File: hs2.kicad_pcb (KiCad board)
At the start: 2 copper layers, 0 parts

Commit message: layout: Components placement
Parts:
- added C1: 47nF, Capacitor_THT:C_Disc_D4.3mm_W1.9mm_P5.00mm, F.Cu at (110.4, 121.7)
- added C10: 1uF, Capacitor_THT:CP_Radial_D5.0mm_P2.50mm, F.Cu at (138.4, 73.9)
- added C11: 1nF, Capacitor_THT:CP_Radial_D5.0mm_P2.50mm, F.Cu at (155.2, 100.1)
- added C12: 1uF, Capacitor_THT:CP_Radial_D5.0mm_P2.50mm, F.Cu at (162.3, 68.3)
- added C13: 470p, Capacitor_THT:C_Disc_D4.3mm_W1.9mm_P5.00mm, F.Cu at (159.2, 104.1)
- added C14: 1.5uF, Capacitor_THT:CP_Radial_D5.0mm_P2.50mm, F.Cu at (126.2, 73.4)
- added C15: 150nF, Capacitor_THT:C_Disc_D4.3mm_W1.9mm_P5.00mm, F.Cu at (144.5, 87.1)
- added C16: 100nF, Capacitor_THT:C_Disc_D4.3mm_W1.9mm_P5.00mm, F.Cu at (144.5, 74.9)
- added C17: 68nF, Capacitor_THT:C_Disc_D4.3mm_W1.9mm_P5.00mm, F.Cu at (123.4, 70.1)
- added C18: 6.8nF, Capacitor_THT:C_Disc_D4.3mm_W1.9mm_P5.00mm, F.Cu at (148.5, 92.5)
- added C19: 4.7nF, Capacitor_THT:C_Disc_D4.3mm_W1.9mm_P5.00mm, F.Cu at (148.0, 72.3)
- added C2: 47nF, Capacitor_THT:C_Disc_D4.3mm_W1.9mm_P5.00mm, F.Cu at (112.2, 95.4)
- added C20: 10uF, Capacitor_THT:CP_Radial_D5.0mm_P2.50mm, F.Cu at (168.3, 101.5)
- added C21: 47n, Capacitor_THT:C_Disc_D4.3mm_W1.9mm_P5.00mm, F.Cu at (154.1, 121.6)
- added C22: 1uF, Capacitor_THT:CP_Radial_D5.0mm_P2.50mm, F.Cu at (168.6, 120.1)
- added C23: 100uF, Capacitor_THT:CP_Radial_D5.0mm_P2.50mm, F.Cu at (154.6, 54.1)
- added C24: 10uF, Capacitor_THT:CP_Radial_D5.0mm_P2.50mm, F.Cu at (133.8, 59.4)
- added C3: 100pF, Capacitor_THT:C_Disc_D4.3mm_W1.9mm_P5.00mm, F.Cu at (111.2, 106.9)
- added C4: 47uF, Capacitor_THT:CP_Radial_D5.0mm_P2.50mm, F.Cu at (111.7, 69.3)
- added C5: 10uF, Capacitor_THT:CP_Radial_D5.0mm_P2.50mm, F.Cu at (107.4, 88.6)
- added C6: 47nF, Capacitor_THT:C_Disc_D4.3mm_W1.9mm_P5.00mm, F.Cu at (104.3, 101.9)
- added C7: 100pF, Capacitor_THT:C_Disc_D4.3mm_W1.9mm_P5.00mm, F.Cu at (138.9, 97.5)
- added C8: 47nF, Capacitor_THT:C_Disc_D4.3mm_W1.9mm_P5.00mm, F.Cu at (120.6, 96.8)
- added C9: 100pF, Capacitor_THT:C_Disc_D4.3mm_W1.9mm_P5.00mm, F.Cu at (155.1, 129.3)
- added D1: 1N4148, Diode_THT:D_DO-35_SOD27_P7.62mm_Horizontal, F.Cu at (144.7, 121.9)
- added D2: 1N4148, Diode_THT:D_DO-35_SOD27_P7.62mm_Horizontal, F.Cu at (141.7, 116.8)
- added D3: 1N4001, Diode_THT:D_DO-41_SOD81_P10.16mm_Horizontal, F.Cu at (151.3, 52.8)
- added D4: 1N4148, Diode_THT:D_DO-35_SOD27_P7.62mm_Horizontal, F.Cu at (141.7, 126.7)
- added D5: DIODE, Diode_THT:D_DO-41_SOD81_P10.16mm_Horizontal, F.Cu at (151.3, 58.7)
- added D6: DIODE, Diode_THT:D_DO-41_SOD81_P10.16mm_Horizontal, F.Cu at (161.5, 62.0)
- added D7: 1N4148, Diode_THT:D_DO-35_SOD27_P7.62mm_Horizontal, F.Cu at (124.9, 125.5)
- added D8: 1N4148, Diode_THT:D_DO-35_SOD27_P7.62mm_Horizontal, F.Cu at (168.1, 68.3)
- added H1: MountingHole_Pad, MountingHole:MountingHole_3.2mm_M3_Pad_TopBottom, F.Cu at (105.4, 54.6)
- added H2: MountingHole_Pad, MountingHole:MountingHole_3.2mm_M3_Pad_TopBottom, F.Cu at (167.8, 54.6)
- added H3: MountingHole_Pad, MountingHole:MountingHole_3.2mm_M3_Pad_TopBottom, F.Cu at (105.4, 132.1)
- added H4: MountingHole_Pad, MountingHole:MountingHole_3.2mm_M3_Pad_TopBottom, F.Cu at (167.8, 132.1)
- added J1: Conn_01x01, Connector_PinHeader_2.54mm:PinHeader_1x01_P2.54mm_Vertical, F.Cu at (103.6, 114.0)
- added J2: Conn_01x01, Connector_PinHeader_2.54mm:PinHeader_1x01_P2.54mm_Vertical, F.Cu at (169.6, 114.0)
- added J3: Conn_01x02, Connector_PinHeader_2.54mm:PinHeader_1x02_P2.54mm_Vertical, F.Cu at (135.3, 53.1)
- added Q1: 2N5457, Package_TO_SOT_THT:TO-92_Inline, F.Cu at (117.5, 114.3)
- added Q2: 2N3904, Package_TO_SOT_THT:TO-92_Inline, F.Cu at (107.5, 107.2)
- added Q3: 2N3906, Package_TO_SOT_THT:TO-92_Inline, F.Cu at (130.0, 87.1)
- added Q4: 2N3904, Package_TO_SOT_THT:TO-92_Inline, F.Cu at (158.4, 120.4)
- added R1: 10k, Resistor_THT:R_Axial_DIN0207_L6.3mm_D2.5mm_P10.16mm_Horizontal, F.Cu at (107.4, 114.0)
- added R10: 10k, Resistor_THT:R_Axial_DIN0207_L6.3mm_D2.5mm_P10.16mm_Horizontal, F.Cu at (111.5, 52.6)
- added R11: 22k, Resistor_THT:R_Axial_DIN0207_L6.3mm_D2.5mm_P10.16mm_Horizontal, F.Cu at (120.6, 94.0)
- added R12: 100k, Resistor_THT:R_Axial_DIN0207_L6.3mm_D2.5mm_P10.16mm_Horizontal, F.Cu at (125.4, 106.9)
- added R13: 470k, Resistor_THT:R_Axial_DIN0207_L6.3mm_D2.5mm_P10.16mm_Horizontal, F.Cu at (135.6, 100.1)
- added R14: 10k, Resistor_THT:R_Axial_DIN0207_L6.3mm_D2.5mm_P10.16mm_Horizontal, F.Cu at (142.2, 100.1)
- added R15: 120, Resistor_THT:R_Axial_DIN0207_L6.3mm_D2.5mm_P10.16mm_Horizontal, F.Cu at (130.8, 90.7)
- added R16: 68k, Resistor_THT:R_Axial_DIN0207_L6.3mm_D2.5mm_P10.16mm_Horizontal, F.Cu at (136.1, 114.0)
- added R17: 47k, Resistor_THT:R_Axial_DIN0207_L6.3mm_D2.5mm_P10.16mm_Horizontal, F.Cu at (117.5, 85.9)
- added R18: 220k, Resistor_THT:R_Axial_DIN0207_L6.3mm_D2.5mm_P10.16mm_Horizontal, F.Cu at (144.7, 124.2)
- added R19: 10k, Resistor_THT:R_Axial_DIN0207_L6.3mm_D2.5mm_P10.16mm_Horizontal, F.Cu at (138.4, 63.0)
- added R2: 1M, Resistor_THT:R_Axial_DIN0207_L6.3mm_D2.5mm_P10.16mm_Horizontal, F.Cu at (113.5, 114.0)
- added R20: 10k, Resistor_THT:R_Axial_DIN0207_L6.3mm_D2.5mm_P10.16mm_Horizontal, F.Cu at (157.9, 73.2)
- added R21: 68k, Resistor_THT:R_Axial_DIN0207_L6.3mm_D2.5mm_P10.16mm_Horizontal, F.Cu at (129.2, 62.7)
- added R22: 3k3, Resistor_THT:R_Axial_DIN0207_L6.3mm_D2.5mm_P10.16mm_Horizontal, F.Cu at (153.4, 92.5)
- added R23: 3k3, Resistor_THT:R_Axial_DIN0207_L6.3mm_D2.5mm_P10.16mm_Horizontal, F.Cu at (156.4, 107.2)
- added R24: 10k, Resistor_THT:R_Axial_DIN0207_L6.3mm_D2.5mm_P10.16mm_Horizontal, F.Cu at (169.4, 95.8)
- added R25: 470k, Resistor_THT:R_Axial_DIN0207_L6.3mm_D2.5mm_P10.16mm_Horizontal, F.Cu at (156.4, 110.5)
- added R26: 10k, Resistor_THT:R_Axial_DIN0207_L6.3mm_D2.5mm_P10.16mm_Horizontal, F.Cu at (168.6, 126.7)
- added R27: 1k, Resistor_THT:R_Axial_DIN0207_L6.3mm_D2.5mm_P10.16mm_Horizontal, F.Cu at (158.4, 123.4)
- added R28: 100k, Resistor_THT:R_Axial_DIN0207_L6.3mm_D2.5mm_P10.16mm_Horizontal, F.Cu at (156.4, 113.8)
- added R29: 100k, Resistor_THT:R_Axial_DIN0207_L6.3mm_D2.5mm_P10.16mm_Horizontal, F.Cu at (113.5, 128.5)
- added R3: 22k, Resistor_THT:R_Axial_DIN0207_L6.3mm_D2.5mm_P10.16mm_Horizontal, F.Cu at (117.5, 98.3)
- added R30: 330, Resistor_THT:R_Axial_DIN0207_L6.3mm_D2.5mm_P10.16mm_Horizontal, F.Cu at (132.0, 74.9)
- added R31: 82k, Resistor_THT:R_Axial_DIN0207_L6.3mm_D2.5mm_P10.16mm_Horizontal, F.Cu at (149.3, 111.3)
- added R32: 330, Resistor_THT:R_Axial_DIN0207_L6.3mm_D2.5mm_P10.16mm_Horizontal, F.Cu at (145.5, 100.1)
- added R33: 100k, Resistor_THT:R_Axial_DIN0207_L6.3mm_D2.5mm_P10.16mm_Horizontal, F.Cu at (135.1, 67.1)
- added R34: 330, Resistor_THT:R_Axial_DIN0207_L6.3mm_D2.5mm_P10.16mm_Horizontal, F.Cu at (151.3, 74.9)
- added R35: 10k, Resistor_THT:R_Axial_DIN0207_L6.3mm_D2.5mm_P10.16mm_Horizontal, F.Cu at (120.9, 56.1)
- added R36: 10k, Resistor_THT:R_Axial_DIN0207_L6.3mm_D2.5mm_P10.16mm_Horizontal, F.Cu at (120.9, 59.4)
- added R38: 330, Resistor_THT:R_Axial_DIN0207_L6.3mm_D2.5mm_P10.16mm_Horizontal, F.Cu at (120.9, 52.8)
- added R4: 10k, Resistor_THT:R_Axial_DIN0207_L6.3mm_D2.5mm_P10.16mm_Horizontal, F.Cu at (122.1, 125.7)
- added R5: 100k, Resistor_THT:R_Axial_DIN0207_L6.3mm_D2.5mm_P10.16mm_Horizontal, F.Cu at (125.4, 119.6)
- added R6: 470k, Resistor_THT:R_Axial_DIN0207_L6.3mm_D2.5mm_P10.16mm_Horizontal, F.Cu at (114.2, 108.5)
- added R7: 22, Resistor_THT:R_Axial_DIN0207_L6.3mm_D2.5mm_P10.16mm_Horizontal, F.Cu at (117.0, 111.3)
- added R8: 150, Resistor_THT:R_Axial_DIN0207_L6.3mm_D2.5mm_P10.16mm_Horizontal, F.Cu at (107.4, 91.7)
- added R9: 1k, Resistor_THT:R_Axial_DIN0207_L6.3mm_D2.5mm_P10.16mm_Horizontal, F.Cu at (115.0, 62.7)
- added U1: Opamp_Dual, Package_SIP:SIP-8_19x3mm_P2.54mm, F.Cu at (136.1, 134.4)
- added U2: Opamp_Dual, Package_SIP:SIP-8_19x3mm_P2.54mm, F.Cu at (148.3, 87.6)
- added U3: Opamp_Dual, Package_SIP:SIP-8_19x3mm_P2.54mm, F.Cu at (149.8, 116.6)
- added VR1: C250k, TerminalBlock:TerminalBlock_bornier-3_P5.08mm, F.Cu at (107.9, 80.3)
- added VR2: B50k, TerminalBlock:TerminalBlock_bornier-3_P5.08mm, F.Cu at (123.6, 80.3)
- added VR3: B50k, TerminalBlock:TerminalBlock_bornier-3_P5.08mm, F.Cu at (139.4, 80.3)
- added VR4: A10k, TerminalBlock:TerminalBlock_bornier-3_P5.08mm, F.Cu at (155.1, 80.3)
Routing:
- net +9V: track 0.00 -> 60.1 mm
- net Net-(C13-Pad2): track 0.00 -> 48.5 mm, vias 0 -> 1
- net GND: track 0.00 -> 47.9 mm
- net Net-(C8-Pad2): track 0.00 -> 40.6 mm
- net Net-(C10-Pad1): track 0.00 -> 33.7 mm
- net Net-(C7-Pad2): track 0.00 -> 30.3 mm
- net Net-(C2-Pad1): track 0.00 -> 27.3 mm
- net /1/2V: track 0.00 -> 21.9 mm
- net Net-(C7-Pad1): track 0.00 -> 20.1 mm
- net Net-(C3-Pad1): track 0.00 -> 19.4 mm
- net Net-(C21-Pad2): track 0.00 -> 17.7 mm
- net Net-(C6-Pad2): track 0.00 -> 17.4 mm
- net Net-(C14-Pad1): track 0.00 -> 15.3 mm
- net Net-(C16-Pad2): track 0.00 -> 13.4 mm
- net Net-(C15-Pad1): track 0.00 -> 12.2 mm
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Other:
- board outline added: 70 x 85 mm

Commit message: layout: Routing finished
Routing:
- net +9V: track 60.1 -> 232.0 mm, vias 0 -> 7
- net /1/2V: track 21.9 -> 148.5 mm, vias 0 -> 5
- net Net-(C17-Pad2): track 0.00 -> 88.9 mm, vias 0 -> 2
- net Net-(C11-Pad1): track 8.13 -> 88.7 mm, vias 0 -> 2
- net Net-(R22-Pad1): track 0.00 -> 75.8 mm, vias 0 -> 2
- net Net-(C13-Pad1): track 4.21 -> 78.4 mm
- net Net-(C12-Pad1): track 0.00 -> 69.6 mm
- net Net-(C19-Pad2): track 2.90 -> 67.9 mm, vias 0 -> 2
- net Net-(C10-Pad1): track 33.7 -> 91.4 mm, vias 0 -> 3
- net Net-(C3-Pad2): track 10.7 -> 65.3 mm
- net Net-(C21-Pad1): track 0.00 -> 52.3 mm
- net Net-(R34-Pad1): track 2.54 -> 50.3 mm, vias 0 -> 1
- net Net-(R32-Pad1): track 2.54 -> 44.3 mm
- net Net-(C18-Pad2): track 0.00 -> 37.3 mm, vias 0 -> 3
- net Net-(C4-Pad1): track 8.09 -> 43.4 mm
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- added copper zone on B.Cu, net GND
- added copper zone on F.Cu, net GND

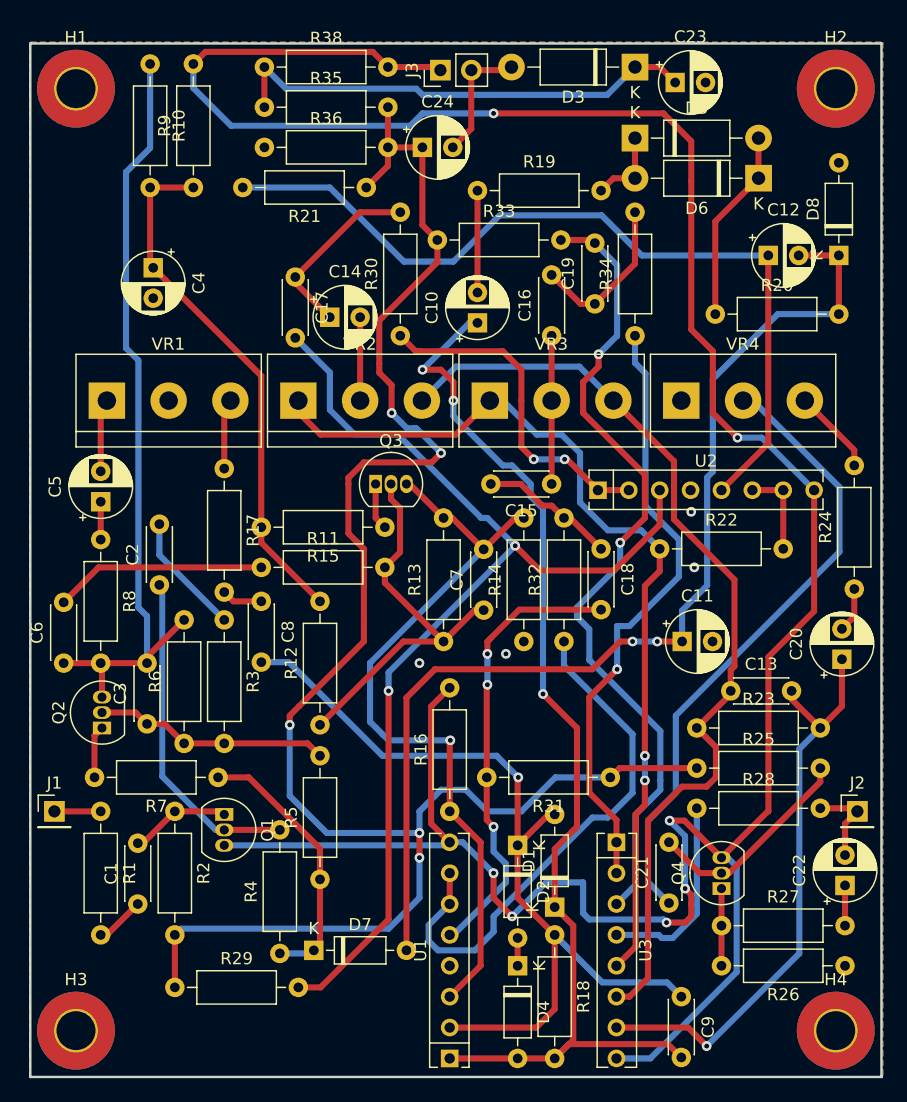
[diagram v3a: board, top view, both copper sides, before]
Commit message: layout: Adding logos and text
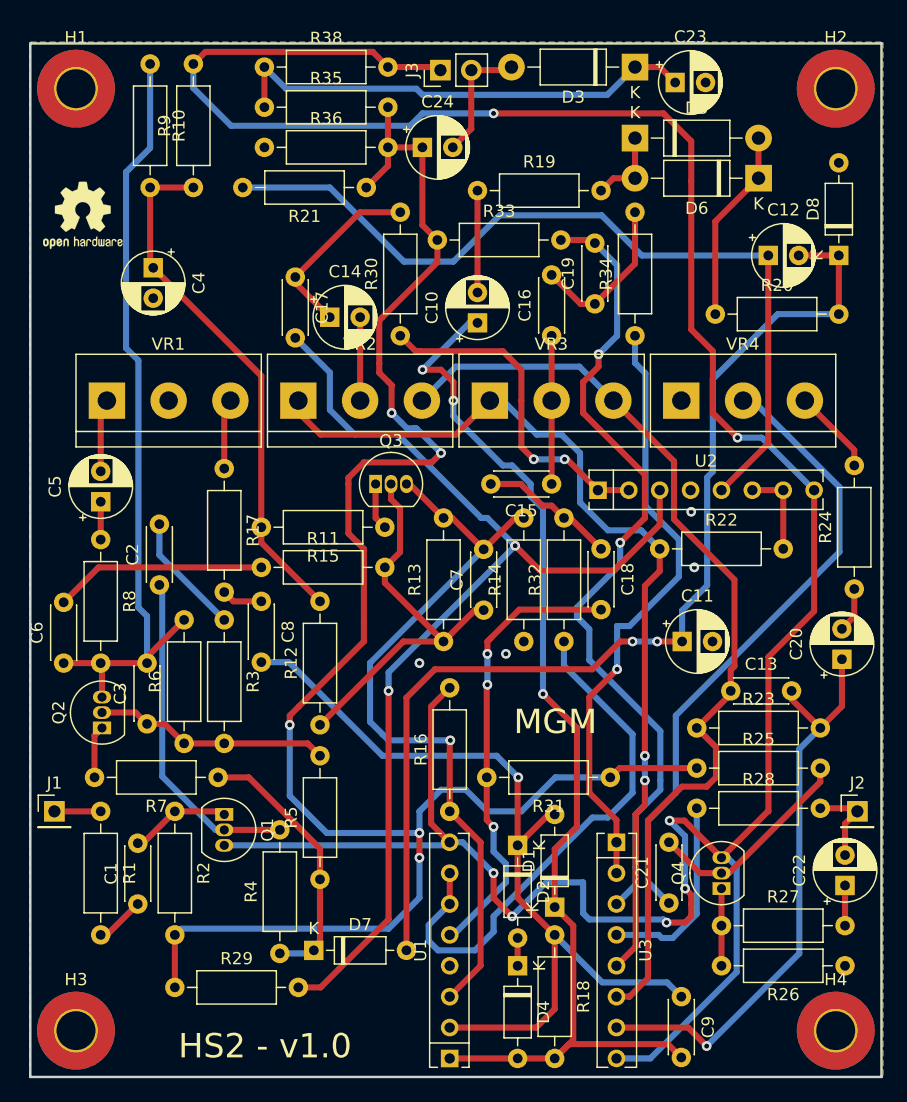
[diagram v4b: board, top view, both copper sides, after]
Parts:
- added REF**: OSHW-Logo2_7.3x6mm_SilkScreen, Symbol:OSHW-Logo2_7.3x6mm_SilkScreen, F.Cu at (105.9, 65.0)
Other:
- board text added: "HS2 - v1.0"
- board text added: "MGM"
